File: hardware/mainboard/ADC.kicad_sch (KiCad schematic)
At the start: 24 parts, among them IC4 ADC 24bit, IC5 LTC1799

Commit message: schematic?
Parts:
- removed C30: 1nF, Capacitor_SMD:C_0603_1608Metric, symbol Device:C_Small
- removed R1: 1M/700V/.1%, Resistor_SMD:R_1206_3216Metric, symbol Device:R_Small
- removed R4: 10k/.1%, Resistor_SMD:R_0603_1608Metric, symbol Device:R_Small
- removed R49, R6: 10k/.1%, Resistor_SMD:R_1206_3216Metric, symbol Device:R_Small
- R24: renamed from R18; value 8.2k -> 25k/.1%
- R33: value 10k/.1% -> 20k/.1%
- R43: footprint Resistor_SMD:R_1206_3216Metric -> Resistor_SMD:R_0603_1608Metric
- renumbered C31 to C45, C34 to C46, C35 to C47, C41 to C48, C49 to C52, IC4 to IC8, IC5 to IC9, R21 to R22
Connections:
- net GNDISO is gone; now on net GND: R43.1
- net ACU+: now also C89.2, IC8.3 (CH1+), R50.1
- net ACU-: now also C89.1, IC8.4 (CH1-), R51.2
- net ACU_V+: now also R50.2
- net ACU_V-: now also R51.1
- net CAR+: now also C90.2, IC8.5 (CH2+), R52.1
- net CAR-: now also C90.1, IC8.6 (CH2-), R54.2
- net CAR_V+: now also R52.2
- net CAR_V-: now also R54.1
- net GND: now also C88.1, IC8.2 (CH0-), IC8.7 (CH3+)
- net I+: now also C88.2, IC8.1 (CH0+), R33.1, R43.2
- net +3.3VISO renamed +3.3VIO
- net +3.3VIO: no longer C45.1, C46.1, IC8.19 (AVDD)
- net 8.192MHZ renamed 4MHz
- new net +3.3VA: C45.1, C46.1, IC8.19 (AVDD)
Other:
- note added: "ADC"
- note added: "CLK GEN"
- note removed: "8.192 CLK GEN"
- note removed: "INPUTS"
- note removed: "ISOLATED ADC"
- moved on the sheet: C88, C89, C90, R24, R33, R43, R50, R51, R52, R54

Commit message: isolation with every thing
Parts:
- added C96: 1nF, Capacitor_SMD:C_0603_1608Metric, symbol Device:C_Small
- added R72: 50k/.1%, Resistor_SMD:R_0603_1608Metric, symbol Device:R_Small
- added R73: 10k/.1%, Resistor_SMD:R_0603_1608Metric, symbol Device:R_Small
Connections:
- net ACU+: now also IC8.5 (CH2+); no longer IC8.3 (CH1+)
- net ACU-: now also IC8.6 (CH2-); no longer IC8.4 (CH1-)
- net CAR+: now also IC8.7 (CH3+); no longer IC8.5 (CH2+)
- net CAR-: now also IC8.8 (CH3-); no longer IC8.6 (CH2-)
- net GND: now also IC8.4 (CH1-), C96.1, R73.1; no longer IC8.7 (CH3+), IC8.8 (CH3-)
- net I+: now also IC8.3 (CH1+); no longer IC8.1 (CH0+)
- new net: C96.2, IC8.1 (CH0+), R72.1, R73.2
- new net +5VA: R72.2
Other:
- moved on the sheet: C45, C46, C47, C48, C52, C88, C89, C90, IC8, IC9, R22, R24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

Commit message: chore: sync
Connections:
- net +5VA_MEAS: now reaches C96.2, IC8.1 (CH0+), R72.1, R73.2
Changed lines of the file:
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@@
+		)
+	)
+	(label "+5VA_MEAS"
+		(at 148.59 83.82 180)
+		(effects
+			(font
+				(size 1.27 1.27)
+			)
+			(justify right bottom)
 		)
 	)

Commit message: Layout again
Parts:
- added TP10, TP11, TP12, TP13, TP14, TP15, TP16, TP8, TP9: TestPoint_Small, TestPoint:TestPoint_Pad_D1.0mm, symbol Connector:TestPoint_Small
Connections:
- net +5VA_MEAS: now also TP8.1
- net 4MHz: now also TP16.1
- net ACU+: now also TP12.1
- net ACU-: now also TP13.1
- net CAR+: now also TP14.1
- net CAR-: now also TP15.1
- net GND: now also TP10.1, TP9.1
- net I+: now also TP11.1

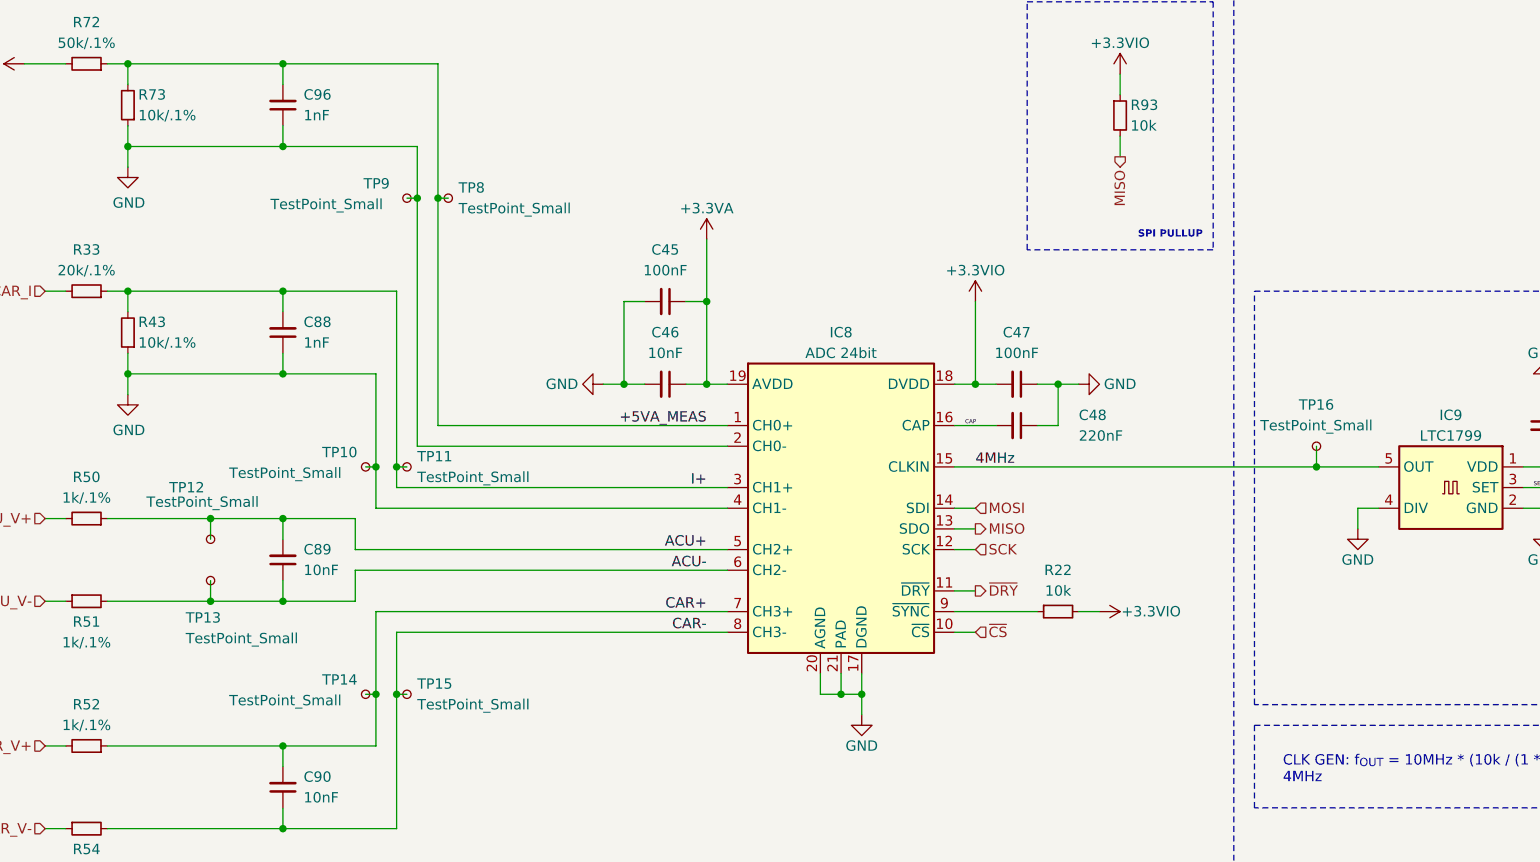
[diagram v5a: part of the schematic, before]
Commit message: Plytka chyba fajnie zrobiona oprocz teardropow bo kicad 10 jest dziwny
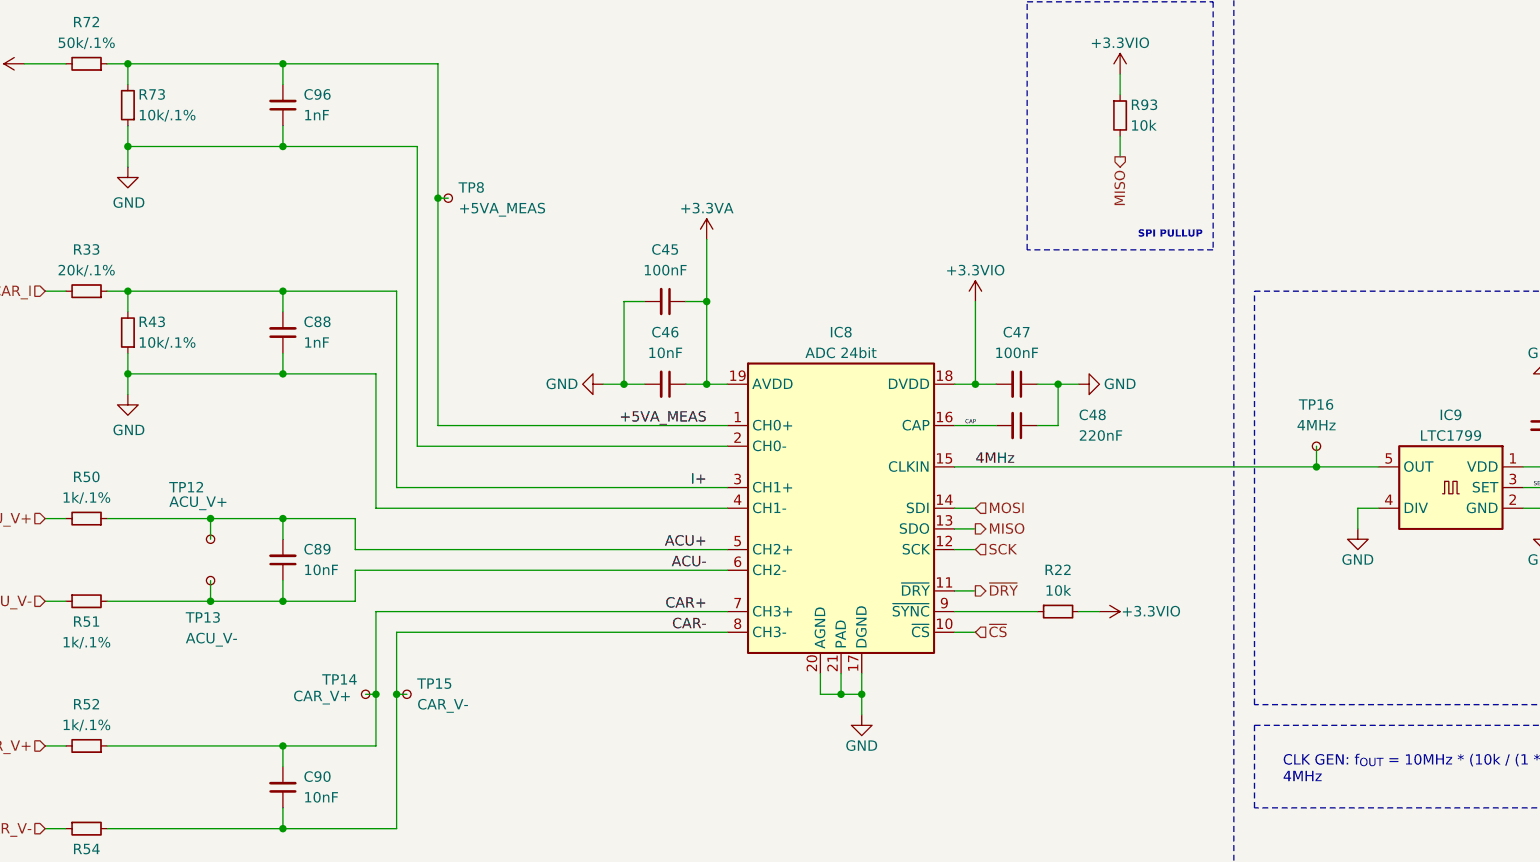
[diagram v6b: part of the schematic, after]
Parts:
- removed TP10, TP11, TP9: TestPoint_Small, TestPoint:TestPoint_Pad_D1.0mm, symbol Connector:TestPoint_Small
- TP12: value TestPoint_Small -> ACU_V+
- TP13: value TestPoint_Small -> ACU_V-
- TP14: value TestPoint_Small -> CAR_V+
- TP15: value TestPoint_Small -> CAR_V-
- TP16: value TestPoint_Small -> 4MHz
- TP8: value TestPoint_Small -> +5VA_MEAS

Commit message: sync
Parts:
- removed TP12: ACU_V+, TestPoint:TestPoint_Pad_D1.0mm, symbol Connector:TestPoint_Small
- removed TP13: ACU_V-, TestPoint:TestPoint_Pad_D1.0mm, symbol Connector:TestPoint_Small
- removed TP14: CAR_V+, TestPoint:TestPoint_Pad_D1.0mm, symbol Connector:TestPoint_Small
- removed TP15: CAR_V-, TestPoint:TestPoint_Pad_D1.0mm, symbol Connector:TestPoint_Small
- removed TP8: +5VA_MEAS, TestPoint:TestPoint_Pad_D1.0mm, symbol Connector:TestPoint_Small
